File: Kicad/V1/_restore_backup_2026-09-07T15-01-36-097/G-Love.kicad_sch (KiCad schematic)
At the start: 12 parts

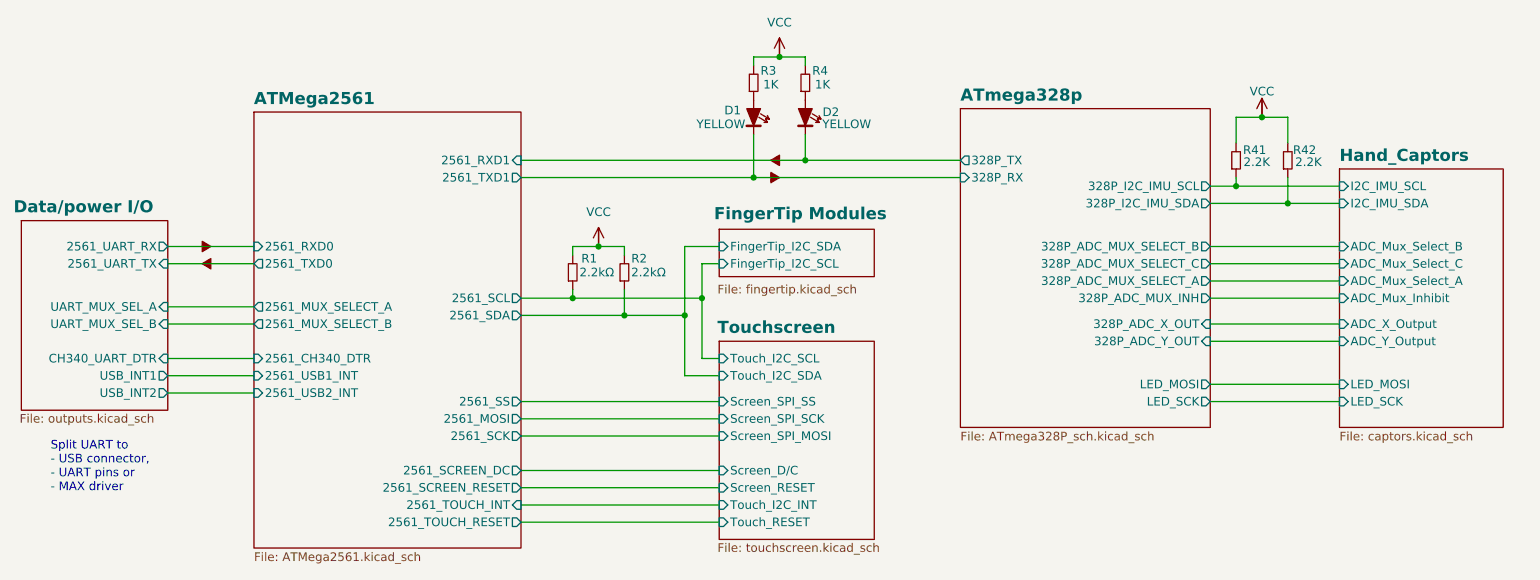
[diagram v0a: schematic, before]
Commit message: correction schema elec + ajout connecteur FPC
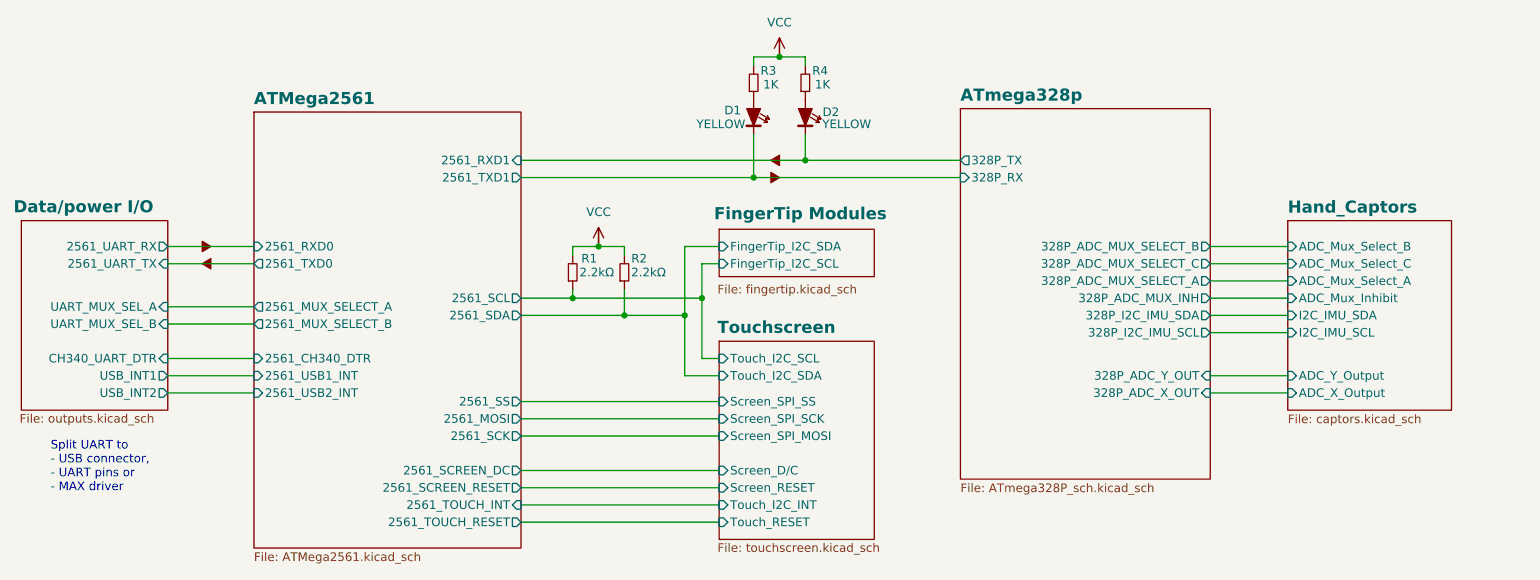
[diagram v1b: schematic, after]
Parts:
- removed R41, R42: 2.2K, symbol G-Love:R
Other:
- sheet ATmega328p ports: added none; removed LED_MOSI, LED_SCK
- sheet Hand_Captors ports: added none; removed LED_MOSI, LED_SCK
